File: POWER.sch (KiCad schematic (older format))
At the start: 27 parts, among them U202 TPS61046, U402 MAX1555

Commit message: modified adui circuit
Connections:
- wire segments 90 -> 62
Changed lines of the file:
@@
 LIBS:mtfc8gacaeam-1m_wt
 LIBS:sn74avc2t244
-LIBS:lsm9ds1
+LIBS:WM8960CGEFL
 LIBS:3210retro-cache
 EELAYER 25 0
@@
 V_USB_BUS_ref
 Wire Wire Line
-	1950 1850 2050 1850
-Wire Wire Line
-	2050 1850 2250 1850
-Wire Wire Line
-	2250 1850 2500 1850
-Wire Wire Line
-	2500 1850 2750 1850
-Wire Wire Line
-	2750 1850 3250 1850
+	1950 1850 3250 1850
 Wire Wire Line
 	2500 1950 2500 1850
 Connection ~ 2500 1850
 Wire Wire Line
-	1950 1200 2250 1200
-Wire Wire Line
-	2250 1200 2500 1200
-Wire Wire Line
-	2500 1200 2750 1200
-Wire Wire Line
-	2750 1200 4300 1200
-Wire Wire Line
-	4300 1200 5000 1200
-Wire Wire Line
-	5000 1200 5950 1200
-Wire Wire Line
-	5950 1200 6450 1200
-Wire Wire Line
-	6450 1200 6550 1200
-Wire Wire Line
-	2050 1300 2050 1500
-Wire Wire Line
-	2050 1500 2050 1550
+	1950 1200 6550 1200
+Wire Wire Line
+	2050 1300 2050 1550
 Wire Wire Line
 	2050 1300 1950 1300
@@
 	2250 1450 2250 1500
 Wire Wire Line
-	2050 1500 2250 1500
-Wire Wire Line
-	2250 1500 2500 1500
-Wire Wire Line
-	2500 1500 2750 1500
+	2050 1500 2750 1500
 Connection ~ 2050 1500
 Wire Wire Line
@@
 Connection ~ 2250 1850
 Wire Wire Line
-	2750 1750 2750 1850
-Wire Wire Line
-	2750 1850 2750 1950
+	2750 1750 2750 1950
 Connection ~ 2750 1850
 Wire Wire Line
 	2250 2150 2250 2200
 Wire Wire Line
-	2250 2200 2500 2200
-Wire Wire Line
-	2500 2200 2750 2200
+	2250 2200 2750 2200
 Wire Wire Line
 	2750 2200 2750 2150
 Wire Wire Line
-	2500 2150 2500 2200
-Wire Wire Line
-	2500 2200 2500 2250
+	2500 2150 2500 2250
 Connection ~ 2500 2200
 Wire Wire Line
-	2050 3450 2050 3650
-Wire Wire Line
-	2050 3650 2050 3700
+	2050 3450 2050 3700
 Wire Wire Line
 	2250 3600 2250 3650
@@
 	4300 1850 4150 1850
 Wire Wire Line
-	1950 3350 2250 3350
-Wire Wire Line
-	2250 3350 2950 3350
-Wire Wire Line
-	2950 2050 2950 3350
-Wire Wire Line
-	2950 3350 2950 3400
+	1950 3350 2950 3350
+Wire Wire Line
+	2950 2050 2950 3400
 Wire Wire Line
 	2950 2050 3250 2050
@@
 	3050 3750 2950 3750
 Wire Wire Line
-	2950 3700 2950 3750
-Wire Wire Line
-	2950 3750 2950 3800
+	2950 3700 2950 3800
 Connection ~ 2950 3750
 Connection ~ 2950 3350
@@
 	5100 1600 5000 1600
 Wire Wire Line
-	5000 1550 5000 1600
-Wire Wire Line
-	5000 1600 5000 1650
+	5000 1550 5000 1650
 Connection ~ 5000 1600
 Wire Wire Line
@@
 	6450 1800 6450 1900
 Wire Wire Line
-	5950 900  5950 1200
-Wire Wire Line
-	5950 1200 5950 1250
+	5950 900  5950 1250
 Connection ~ 5950 1200
 Wire Wire Line
 	7450 1500 7700 1500
 Wire Wire Line
-	8150 1700 8150 1800
-Wire Wire Line
-	8150 1800 8150 1900
+	8150 1700 8150 1900
 Wire Wire Line
 	8150 1300 8150 1400
@@
 Connection ~ 8150 1300
 Wire Wire Line
-	8900 1300 8900 1450
+	8900 1200 8900 1450
 Connection ~ 8500 1300
 Wire Wire Line
@@
 	2050 2950 2050 2900
 Wire Wire Line
-	2050 2200 2050 2500
-Wire Wire Line
-	2050 2500 2050 2600
+	2050 2200 2050 2600
 Wire Wire Line
 	2150 2500 2050 2500
@@
 	7600 900  7250 900
 Wire Wire Line
-	7700 1300 8150 1300
-Wire Wire Line
-	8150 1300 8500 1300
-Wire Wire Line
-	8500 1300 8900 1300
-Wire Wire Line
-	8900 1300 8900 1200
+	7700 1300 8900 1300
 Wire Wire Line
 	7700 1500 7700 1300

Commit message: Added boost converter to battery circuit
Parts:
- removed U202: TPS61046, TO_SOT_Packages_SMD:SOT-23-5, symbol TPS61046
- added U?: TPS61021A, symbol TPS61021A
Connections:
- wire segments 62 -> 69
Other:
- note added: "2.4V"
- moved on the sheet: C231, C413, R412, R413, TP209, TP212, TP213
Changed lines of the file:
@@
 LIBS:sn74avc2t244
 LIBS:WM8960CGEFL
+LIBS:tps61021a
 LIBS:3210retro-cache
 EELAYER 25 0
@@
 L GND #PWR09
 U 1 1 580D3250
-P 6450 1900
-F 0 "#PWR09" H 6450 1650 50  0001 C CNN
-F 1 "GND" H 6450 1750 50  0000 C CNN
-F 2 "" H 6450 1900 50  0000 C CNN
-F 3 "" H 6450 1900 50  0000 C CNN
-	1    6450 1900
+P 6450 2150
+F 0 "#PWR09" H 6450 1900 50  0001 C CNN
+F 1 "GND" H 6450 2000 50  0000 C CNN
+F 2 "" H 6450 2150 50  0000 C CNN
+F 3 "" H 6450 2150 50  0000 C CNN
+	1    6450 2150
 	1    0    0    -1
 $EndComp
@@
 L R R412
 U 1 1 580D38A4
-P 8150 1550
-F 0 "R412" V 8230 1550 50  0000 C CNN
-F 1 "R" V 8150 1550 50  0000 C CNN
-F 2 "Resistors_SMD:R_0603" V 8080 1550 50  0001 C CNN
-F 3 "" H 8150 1550 50  0000 C CNN
-	1    8150 1550
+P 8250 1650
+F 0 "R412" V 8330 1650 50  0000 C CNN
+F 1 "R" V 8250 1650 50  0000 C CNN
+F 2 "Resistors_SMD:R_0603" V 8180 1650 50  0001 C CNN
+F 3 "" H 8250 1650 50  0000 C CNN
+	1    8250 1650
 	-1   0    0    1
 $EndComp
@@
 L R R413
 U 1 1 580D3905
-P 8150 2050
-F 0 "R413" V 8230 2050 50  0000 C CNN
-F 1 "R" V 8150 2050 50  0000 C CNN
-F 2 "Resistors_SMD:R_0603" V 8080 2050 50  0001 C CNN
-F 3 "" H 8150 2050 50  0000 C CNN
-	1    8150 2050
+P 8250 2150
+F 0 "R413" V 8330 2150 50  0000 C CNN
+F 1 "R" V 8250 2150 50  0000 C CNN
+F 2 "Resistors_SMD:R_0603" V 8180 2150 50  0001 C CNN
+F 3 "" H 8250 2150 50  0000 C CNN
+	1    8250 2150
 	-1   0    0    1
 $EndComp
@@
 L C_Small C413
 U 1 1 580D3A62
-P 8500 1550
-F 0 "C413" H 8510 1620 50  0000 L CNN
-F 1 "22p" H 8510 1470 50  0000 L CNN
-F 2 "Capacitors_SMD:C_0603" H 8500 1550 50  0001 C CNN
-F 3 "" H 8500 1550 50  0000 C CNN
-	1    8500 1550
+P 8600 1650
+F 0 "C413" H 8610 1720 50  0000 L CNN
+F 1 "22p" H 8610 1570 50  0000 L CNN
+F 2 "Capacitors_SMD:C_0603" H 8600 1650 50  0001 C CNN
+F 3 "" H 8600 1650 50  0000 C CNN
+	1    8600 1650
 	1    0    0    -1
 $EndComp
@@
 L GND #PWR011
 U 1 1 580D3D8A
-P 8900 1750
-F 0 "#PWR011" H 8900 1500 50  0001 C CNN
-F 1 "GND" H 8900 1600 50  0000 C CNN
-F 2 "" H 8900 1750 50  0000 C CNN
-F 3 "" H 8900 1750 50  0000 C CNN
-	1    8900 1750
+P 9000 1850
+F 0 "#PWR011" H 9000 1600 50  0001 C CNN
+F 1 "GND" H 9000 1700 50  0000 C CNN
+F 2 "" H 9000 1850 50  0000 C CNN
+F 3 "" H 9000 1850 50  0000 C CNN
+	1    9000 1850
 	1    0    0    -1
 $EndComp
@@
 L +4V #PWR012
 U 1 1 580D3E4B
-P 8900 1200
-F 0 "#PWR012" H 8900 1050 50  0001 C CNN
-F 1 "+4V" H 8900 1340 50  0000 C CNN
-F 2 "" H 8900 1200 50  0000 C CNN
-F 3 "" H 8900 1200 50  0000 C CNN
-	1    8900 1200
+P 9000 1300
+F 0 "#PWR012" H 9000 1150 50  0001 C CNN
+F 1 "+4V" H 9000 1440 50  0000 C CNN
+F 2 "" H 9000 1300 50  0000 C CNN
+F 3 "" H 9000 1300 50  0000 C CNN
+	1    9000 1300
 	1    0    0    -1
 $EndComp
@@
 L GND #PWR013
 U 1 1 580D3EFA
-P 8150 2250
-F 0 "#PWR013" H 8150 2000 50  0001 C CNN
-F 1 "GND" H 8150 2100 50  0000 C CNN
-F 2 "" H 8150 2250 50  0000 C CNN
-F 3 "" H 8150 2250 50  0000 C CNN
-	1    8150 2250
+P 8250 2400
+F 0 "#PWR013" H 8250 2150 50  0001 C CNN
+F 1 "GND" H 8250 2250 50  0000 C CNN
+F 2 "" H 8250 2400 50  0000 C CNN
+F 3 "" H 8250 2400 50  0000 C CNN
+	1    8250 2400
 	1    0    0    -1
 $EndComp
@@
 	4300 2250 4150 2250
 Wire Wire Line
-	7600 1200 7600 900
-Wire Wire Line
-	7450 1200 7600 1200
-Connection ~ 7600 900
-Wire Wire Line
-	6550 1800 6450 1800
-Wire Wire Line
-	6450 1800 6450 1900
+	7750 1200 7750 900
+Wire Wire Line
+	7550 1200 7750 1200
+Connection ~ 7750 900
+Wire Wire Line
+	6550 2050 6450 2050
+Wire Wire Line
+	6450 2050 6450 2150
 Wire Wire Line
 	5950 900  5950 1250
 Connection ~ 5950 1200
 Wire Wire Line
-	7450 1500 7700 1500
-Wire Wire Line
-	8150 1700 8150 1900
-Wire Wire Line
-	8150 1300 8150 1400
-Wire Wire Line
-	8500 1300 8500 1450
-Connection ~ 8150 1300
-Wire Wire Line
-	8900 1200 8900 1450
-Connection ~ 8500 1300
-Wire Wire Line
-	8900 1750 8900 1650
-Connection ~ 8900 1300
-Wire Wire Line
-	8150 2250 8150 2200
-Wire Wire Line
-	7450 1800 8150 1800
-Connection ~ 8150 1800
+	7550 1600 7800 1600
+Wire Wire Line
+	8250 1800 8250 2000
+Wire Wire Line
+	8250 1400 8250 1500
+Wire Wire Line
+	8600 1400 8600 1550
+Connection ~ 8250 1400
+Wire Wire Line
+	9000 1300 9000 1550
+Connection ~ 8600 1400
+Wire Wire Line
+	9000 1850 9000 1750
+Connection ~ 9000 1400
+Wire Wire Line
+	8250 2300 8250 2400
+Wire Wire Line
+	7550 1900 8250 1900
+Connection ~ 8250 1900
 Connection ~ 5000 1200
 Wire Wire Line
@@
 L TP TP209
 U 1 1 585B2C55
-P 7600 900
-F 0 "TP209" H 7600 940 20  0000 C CNN
-F 1 "TP" H 7600 850 60  0001 C CNN
-F 2 "buttons:TP" H 7600 900 60  0001 C CNN
-F 3 "" H 7600 900 60  0000 C CNN
-	1    7600 900
+P 7750 900
+F 0 "TP209" H 7750 940 20  0000 C CNN
+F 1 "TP" H 7750 850 60  0001 C CNN
+F 2 "buttons:TP" H 7750 900 60  0001 C CNN
+F 3 "" H 7750 900 60  0000 C CNN
+	1    7750 900
 	1    0    0    -1
 $EndComp
@@
 L TP TP213
 U 1 1 585B2F1F
-P 8150 1800
-F 0 "TP213" H 8150 1840 20  0000 C CNN
-F 1 "TP" H 8150 1750 60  0001 C CNN
-F 2 "buttons:TP" H 8150 1800 60  0001 C CNN
-F 3 "" H 8150 1800 60  0000 C CNN
-	1    8150 1800
+P 8250 1900
+F 0 "TP213" H 8250 1940 20  0000 C CNN
+F 1 "TP" H 8250 1850 60  0001 C CNN
+F 2 "buttons:TP" H 8250 1900 60  0001 C CNN
+F 3 "" H 8250 1900 60  0000 C CNN
+	1    8250 1900
 	1    0    0    -1
 $EndComp
@@
 L TP TP212
 U 1 1 585B2FB4
-P 8150 1300
-F 0 "TP212" H 8150 1340 20  0000 C CNN
-F 1 "TP" H 8150 1250 60  0001 C CNN
-F 2 "buttons:TP" H 8150 1300 60  0001 C CNN
-F 3 "" H 8150 1300 60  0000 C CNN
-	1    8150 1300
+P 8250 1400
+F 0 "TP212" H 8250 1440 20  0000 C CNN
+F 1 "TP" H 8250 1350 60  0001 C CNN
+F 2 "buttons:TP" H 8250 1400 60  0001 C CNN
+F 3 "" H 8250 1400 60  0000 C CNN
+	1    8250 1400
 	1    0    0    -1
 $EndComp
@@
 Connection ~ 2750 1200
 $Comp
-L TPS61046 U202
-U 1 1 5861E06C
-P 7000 1500
-F 0 "U202" H 7200 1950 60  0000 C CNN
-F 1 "TPS61046" H 7000 1650 60  0000 C CNN
-F 2 "TO_SOT_Packages_SMD:SOT-23-5" H 7000 1700 60  0001 C CNN
-F 3 "" H 7000 1700 60  0000 C CNN
-	1    7000 1500
-	1    0    0    -1
-$EndComp
-$Comp
 L GND #PWR034
 U 1 1 5861EE0D
-P 8500 1750
-F 0 "#PWR034" H 8500 1500 50  0001 C CNN
-F 1 "GND" H 8500 1600 50  0000 C CNN
-F 2 "" H 8500 1750 50  0000 C CNN
-F 3 "" H 8500 1750 50  0000 C CNN
-	1    8500 1750
-	1    0    0    -1
-$EndComp
-Wire Wire Line
-	8500 1750 8500 1650
-Wire Wire Line
-	7600 900  7250 900
-Wire Wire Line
-	7700 1300 8900 1300
-Wire Wire Line
-	7700 1500 7700 1300
+P 8600 1850
+F 0 "#PWR034" H 8600 1600 50  0001 C CNN
+F 1 "GND" H 8600 1700 50  0000 C CNN
+F 2 "" H 8600 1850 50  0000 C CNN
+F 3 "" H 8600 1850 50  0000 C CNN
+	1    8600 1850
+	1    0    0    -1
+$EndComp
+Wire Wire Line
+	8600 1850 8600 1750
+Wire Wire Line
+	7750 900  7250 900
+Wire Wire Line
+	7800 1400 9000 1400
+Wire Wire Line
+	7800 1600 7800 1400
 Wire Wire Line
 	6750 900  5950 900
 Wire Wire Line
-	6550 1500 6450 1500
-Wire Wire Line
-	6450 1500 6450 1200
+	6450 1600 6550 1600
+Wire Wire Line
+	6450 1200 6450 1600
 Connection ~ 6450 1200
 $Comp
 L C_Small C231
 U 1 1 585E728C
-P 8900 1550
-F 0 "C231" H 8910 1620 50  0000 L CNN
-F 1 "1u" H 8910 1470 50  0000 L CNN
-F 2 "Capacitors_SMD:C_0603" H 8900 1550 50  0001 C CNN
-F 3 "" H 8900 1550 50  0000 C CNN
-	1    8900 1550
-	1    0    0    -1
-$EndComp
+P 9000 1650
+F 0 "C231" H 9010 1720 50  0000 L CNN
+F 1 "1u" H 9010 1570 50  0000 L CNN
+F 2 "Capacitors_SMD:C_0603" H 9000 1650 50  0001 C CNN
+F 3 "" H 9000 1650 50  0000 C CNN
+	1    9000 1650
+	1    0    0    -1
+$EndComp
+Text Notes 2000 1150 0    60   ~ 0
+2.4V
+$Comp
+L TPS61021A U?
+U 1 1 59460445
+P 7050 1500
+F 0 "U?" H 7250 1950 60  0000 C CNN
+F 1 "TPS61021A" H 7050 1550 60  0000 C CNN
+F 2 "" H 7050 1700 60  0000 C CNN
+F 3 "" H 7050 1700 60  0000 C CNN
+	1    7050 1500
+	1    0    0    -1
+$EndComp
+Wire Wire Line
+	7550 1300 7650 1300
+Wire Wire Line
+	7650 1300 7650 1200
+Connection ~ 7650 1200
+Wire Wire Line
+	7550 1700 7650 1700
+Wire Wire Line
+	7650 1700 7650 1600
+Connection ~ 7650 1600
+Wire Wire Line
+	8250 2350 7650 2350
+Wire Wire Line
+	7650 2350 7650 2050
+Wire Wire Line
+	7650 2050 7550 2050
+Connection ~ 8250 2350
 $EndSCHEMATC

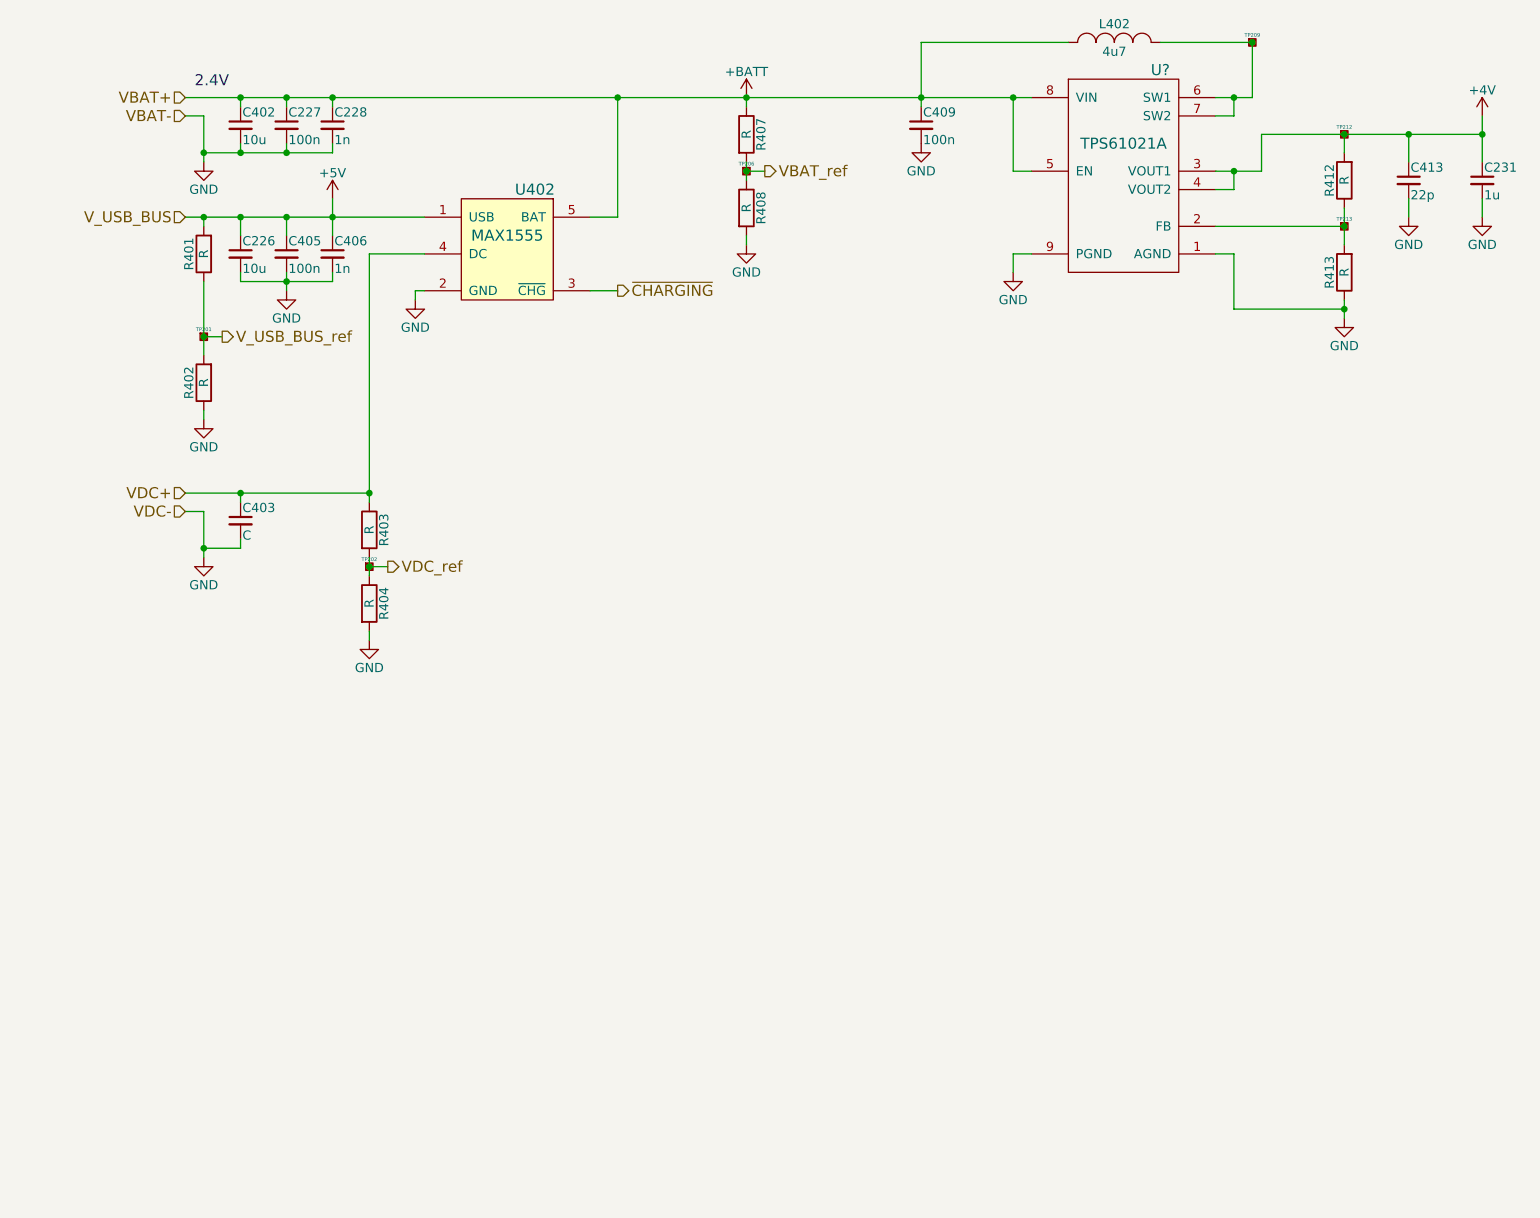
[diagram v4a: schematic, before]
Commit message: Prepare for two battery types NiMH battery for using the original battery pack LiPo battery for using long lasting modern battery
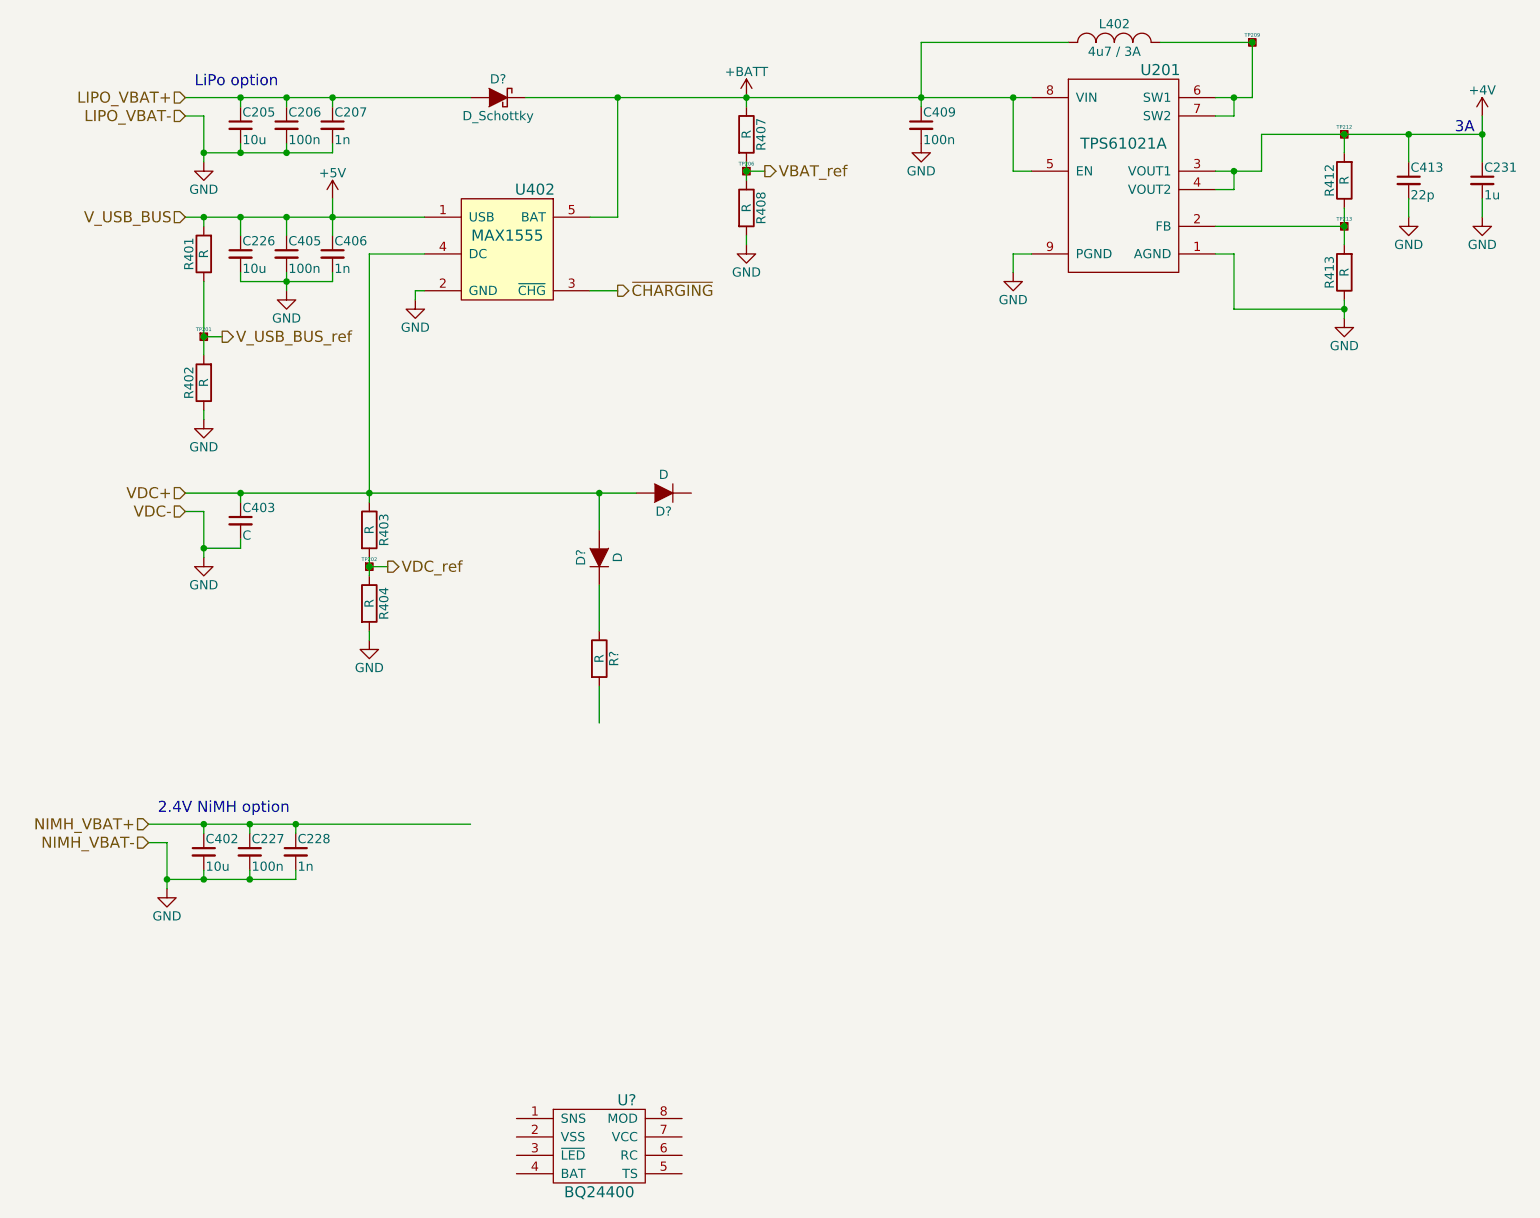
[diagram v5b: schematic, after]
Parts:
- added C205: 10u, Capacitors_SMD:C_0603, symbol C_Small
- added C206: 100n, Capacitors_SMD:C_0603, symbol C_Small
- added C207: 1n, Capacitors_SMD:C_0603, symbol C_Small
- added D? (x2): D, symbol D
- added D?: D_Schottky, symbol D_Schottky
- added R?: R, Resistors_SMD:R_0603, symbol R
- added U?: BQ24400, symbol BQ24400
- L402: value 4u7 -> 4u7 / 3A
- gave numbers to parts that had none: 1
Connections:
- net +BATT: now also D?.1 (K); no longer C227.1, C228.1, C402.1
- net GND: now also C205.2, C206.2, C207.2
- net VDC+: now also D?.2 (A), D?.2 (A)
- new net: D?.1 (K), R?.1
- new net LIPO_VBAT+: C205.1, C206.1, C207.1, D?.2 (A)
- new net NIMH_VBAT+: C227.1, C228.1, C402.1
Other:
- note added: "2.4V NiMH option"
- note added: "3A"
- note added: "LiPo option"
- note removed: "2.4V"
- moved on the sheet: C227, C228, C402
